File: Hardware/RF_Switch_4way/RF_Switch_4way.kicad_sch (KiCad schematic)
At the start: 52 parts, among them J11 Conn_01x08_Pin, K1 G2RL-1-E, K10 G2RL-1-E, K2 G2RL-1-E, K3 G2RL-1-E, K4 G2RL-1-E, K5 G2RL-1-E, K6 G2RL-1-E, K7 G2RL-1-E, K8 G2RL-1-E, K9 G2RL-1-E

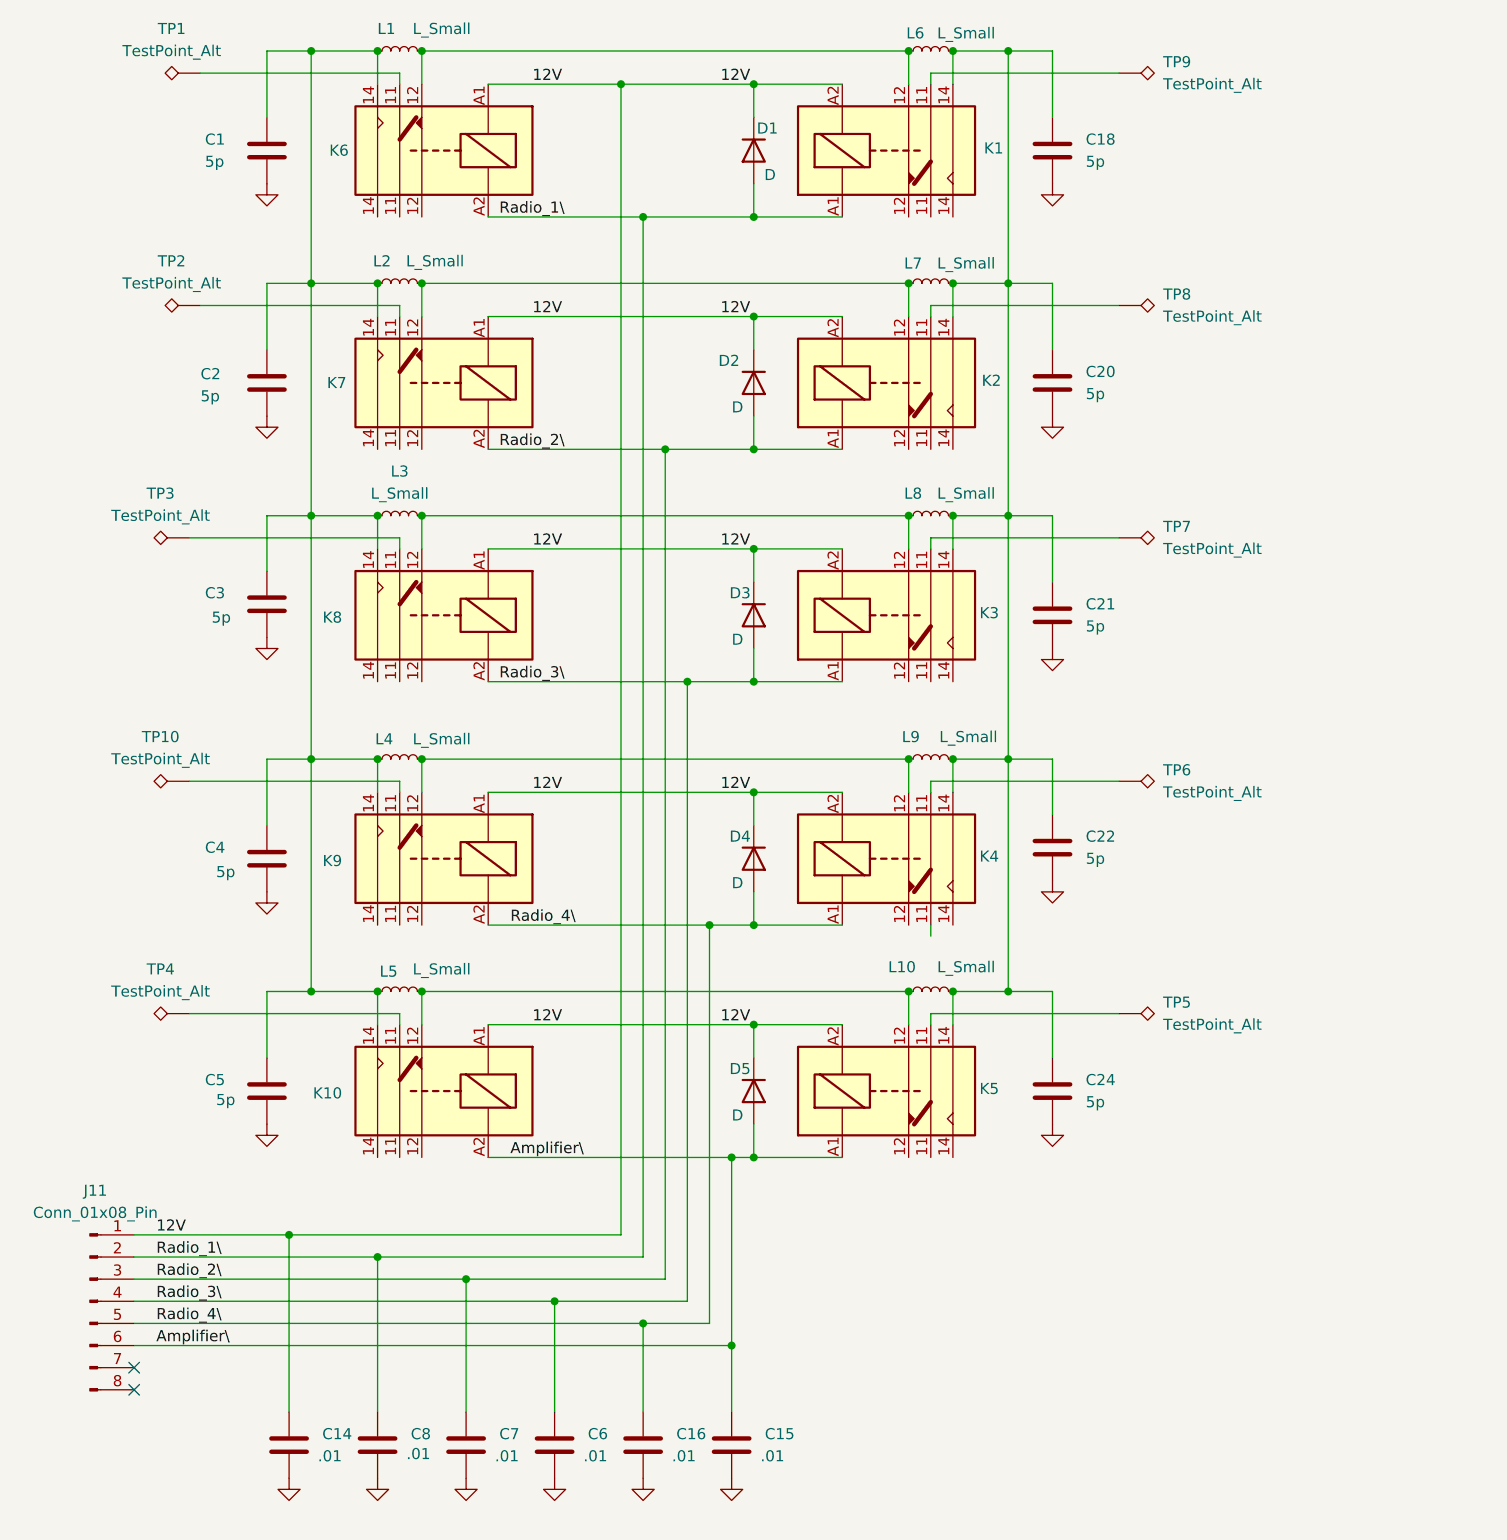
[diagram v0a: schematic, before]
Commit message: Moved 4:1 up a level
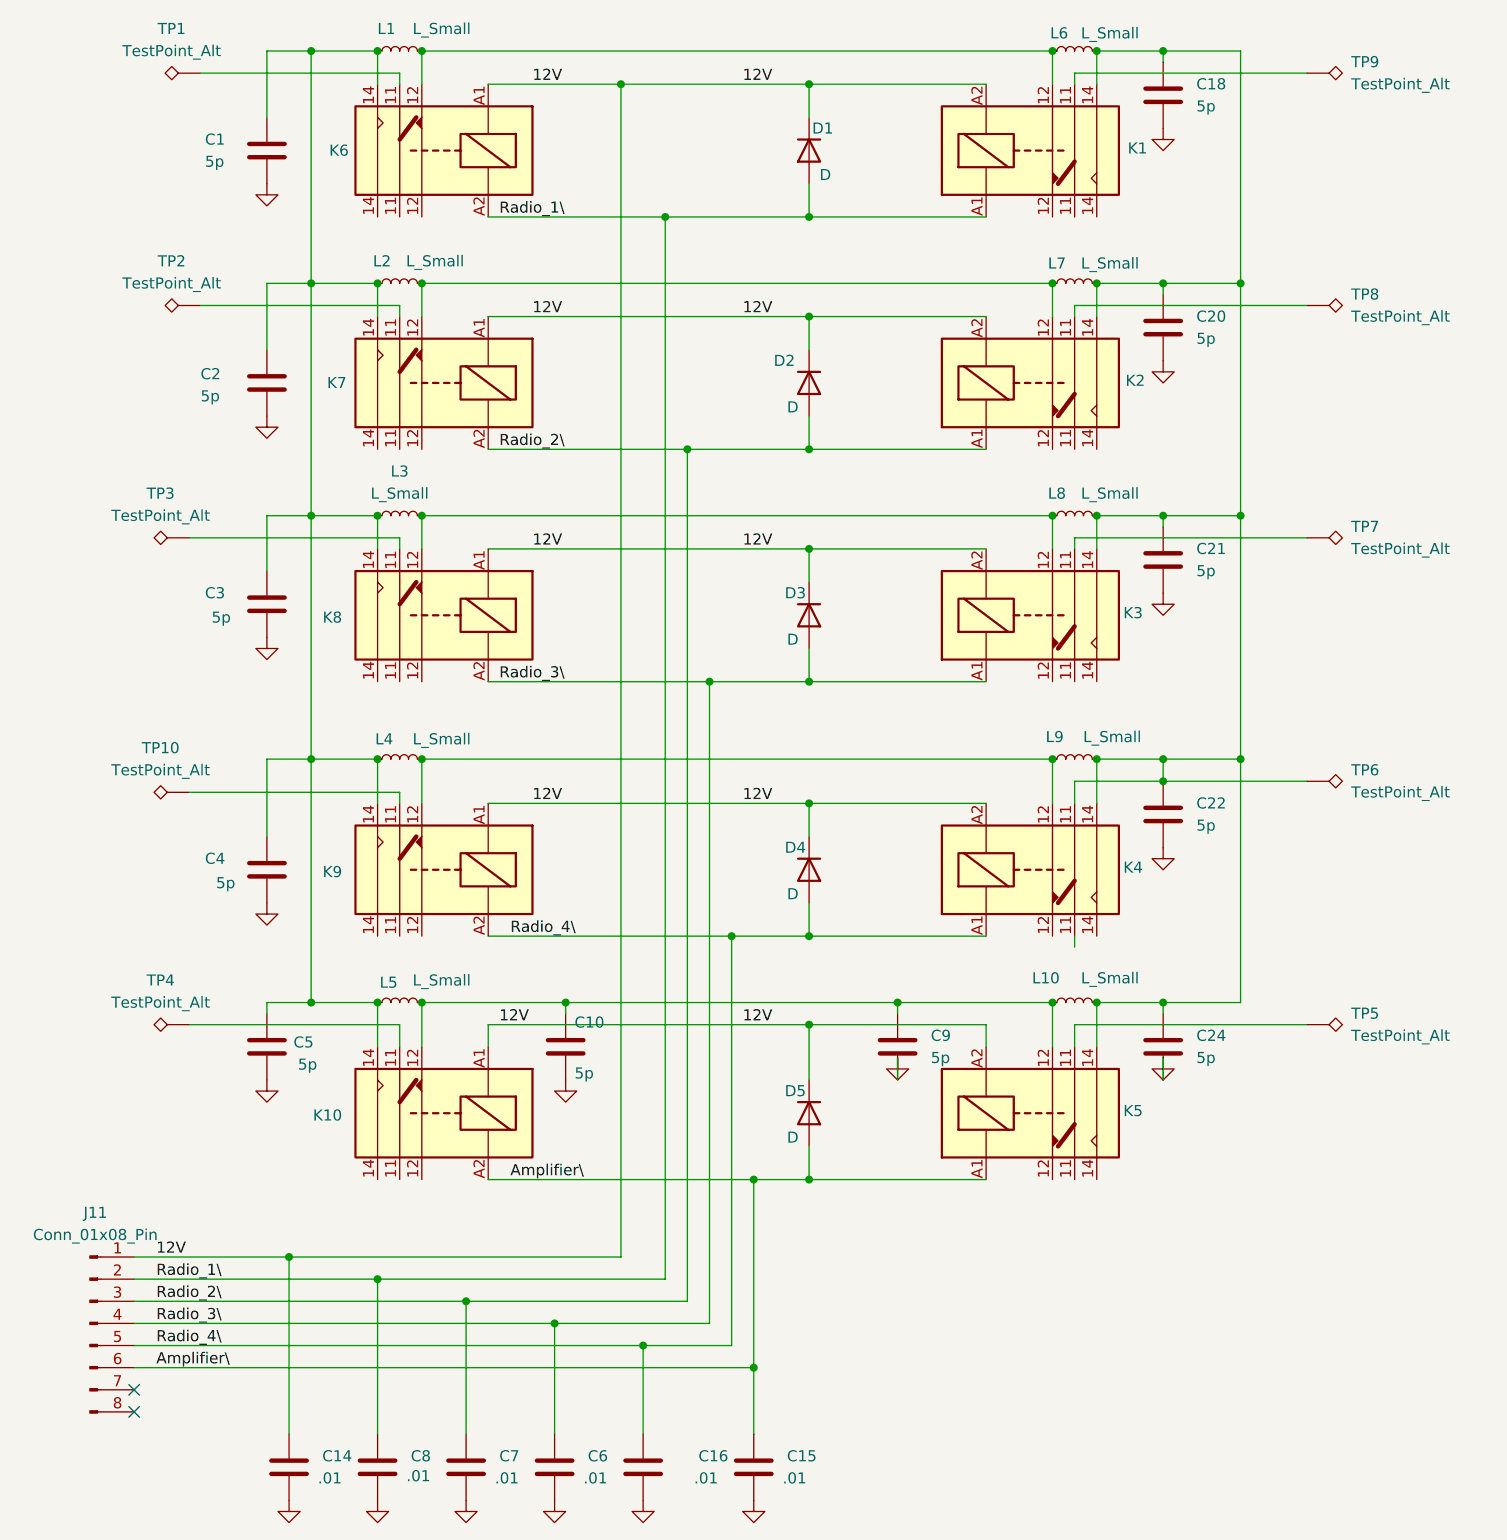
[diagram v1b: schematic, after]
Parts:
- added C10, C9: 5p, Capacitor_SMD:C_0805_2012Metric, symbol Device:C
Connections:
- net GND: now also C10.2, C9.2
- net at K3.11: now also TP7.1
- net at K3.12: now also K8.12, L3.2, L8.1
- net at K3.14: now also C18.1, C20.1, C21.1, C22.1, C24.1, K1.14, K2.14, K4.11, K4.14, K5.14, L10.2, L6.2, L7.2, L8.2, L9.2, TP6.1
- net at K2.11: now also TP8.1
- net at K7.11: now also TP2.1
- net at K1.12: now also K6.12, L1.2, L6.1
- net at K10.12, K5.12, L10.1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: now also C10.1, C9.1
- now unconnected: K1.14, K2.14, K4.11, K4.14, K5.14, K6.12, K8.12
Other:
- moved on the sheet: C14, C15, C16, C18, C20, C21, C22, C24, C4, C5, C6, C7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
